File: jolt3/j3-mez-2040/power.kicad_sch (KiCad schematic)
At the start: 9 parts, among them J29 USB_C_Receptacle_USB2.0_14P, J30 Conn_ARM_JTAG_SWD_10, U2 AP2112-M3.3

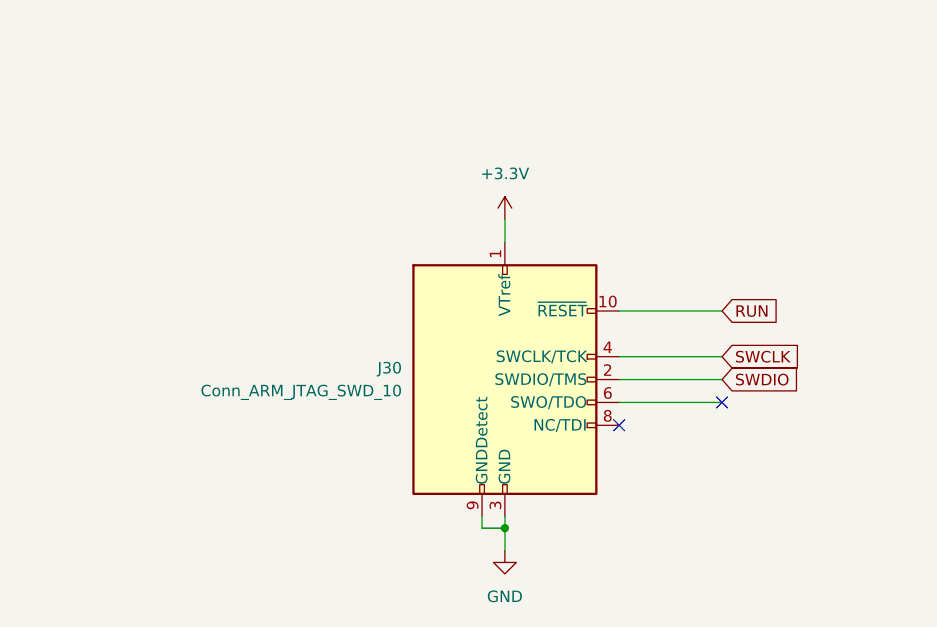
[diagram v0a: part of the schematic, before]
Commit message: Jolt 3: Rev A for 3 boards
Send Rev A out for jolt3-left, jolt3-right, and j3-mez-2040.
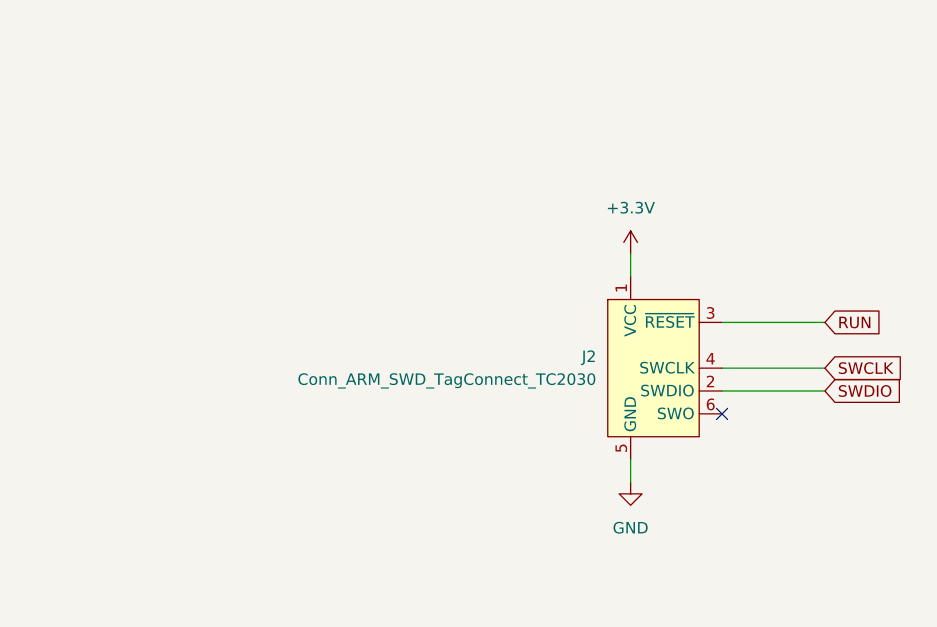
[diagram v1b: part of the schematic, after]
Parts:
- removed J30: Conn_ARM_JTAG_SWD_10, davidb-keyboard-foot:Cortex-M-Debug10, symbol David Brown Keyboard Parts:Conn_ARM_JTAG_SWD_10
- added J2: Conn_ARM_SWD_TagConnect_TC2030, Connector:Tag-Connect_TC2030-IDC-FP_2x03_P1.27mm_Vertical, symbol Connector:Conn_ARM_SWD_TagConnect_TC2030
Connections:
- net +3.3V: now also J2.1 (VCC)
- net GND: now also J2.5 (GND)
- net RUN: now also J2.3 (~{RESET})
- net SWCLK: now also J2.4 (SWCLK)
- net SWDIO: now also J2.2 (SWDIO)
- no-connect marks 3 -> 2
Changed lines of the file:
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@@
-	)
-	(junction
-		(at 156.21 135.89)
-		(diameter 0)
-		(color 0 0 0 0)
 	)
 	(junction
@@
 	)
 	(no_connect
-		(at 168.91 124.46)
+		(at 86.36 125.73)
 	)
 	(no_connect
-		(at 86.36 125.73)
-	)
-	(no_connect
-		(at 180.34 121.92)
+		(at 180.34 123.19)
 	)
 	(wire
@@
 	(wire
 		(pts
-			(xy 156.21 101.6) (xy 156.21 104.14)
+			(xy 170.18 105.41) (xy 170.18 107.95)
+		)
+		(stroke
+			(width 0)
+			(type default)
+		)
+	)
+	(wire
+		(pts
+			(xy 170.18 128.27) (xy 170.18 130.81)
 		)
 		(stroke
@@
 	(wire
 		(pts
-			(xy 168.91 111.76) (xy 180.34 111.76)
-		)
-		(stroke
-			(width 0)
-			(type default)
-		)
-	)
-	(wire
-		(pts
-			(xy 168.91 116.84) (xy 180.34 116.84)
-		)
-		(stroke
-			(width 0)
-			(type default)
-		)
-	)
-	(wire
-		(pts
-			(xy 156.21 135.89) (xy 156.21 138.43)
+			(xy 180.34 113.03) (xy 191.77 113.03)
+		)
+		(stroke
+			(width 0)
+			(type default)
+		)
+	)
+	(wire
+		(pts
+			(xy 180.34 118.11) (xy 191.77 118.11)
 		)
 		(stroke
@@
 	(wire
 		(pts
-			(xy 168.91 121.92) (xy 180.34 121.92)
-		)
-		(stroke
-			(width 0)
-			(type default)
-		)
-	)
-	(wire
-		(pts
 			(xy 78.74 133.35) (xy 78.74 134.62)
 		)
@@
 	(wire
 		(pts
-			(xy 153.67 134.62) (xy 153.67 135.89)
-		)
-		(stroke
-			(width 0)
-			(type default)
-		)
-	)
-	(wire
-		(pts
 			(xy 67.31 66.04) (xy 69.85 66.04)
 		)
@@
 	(wire
 		(pts
-			(xy 156.21 134.62) (xy 156.21 135.89)
-		)
-		(stroke
-			(width 0)
-			(type default)
-		)
-	)
-	(wire
-		(pts
 			(xy 69.85 66.04) (xy 69.85 63.5)
 		)
@@
 	(wire
 		(pts
-			(xy 153.67 135.89) (xy 156.21 135.89)
-		)
-		(stroke
-			(width 0)
-			(type default)
-		)
-	)
-	(wire
-		(pts
 			(xy 93.98 50.8) (xy 128.27 50.8)
 		)
@@
 	(wire
 		(pts
-			(xy 168.91 119.38) (xy 180.34 119.38)
+			(xy 180.34 120.65) (xy 191.77 120.65)
 		)
 		(stroke
@@
 	(global_label "SWCLK"
 		(shape input)
-		(at 180.34 116.84 0)
+		(at 191.77 118.11 0)
 		(fields_autoplaced yes)
 		(effects
@@
 		)
 		(property "Intersheetrefs" "${INTERSHEET_REFS}"
-			(at 189.5542 116.84 0)
+			(at 200.9842 118.11 0)
 			(effects
 				(font
@@
 	(global_label "SWDIO"
 		(shape input)
-		(at 180.34 119.38 0)
+		(at 191.77 120.65 0)
 		(fields_autoplaced yes)
 		(effects
@@
 		)
 		(property "Intersheetrefs" "${INTERSHEET_REFS}"
-			(at 189.1914 119.38 0)
+			(at 200.6214 120.65 0)
 			(effects
 				(font
@@
 	(global_label "RUN"
 		(shape input)
-		(at 180.34 111.76 0)
+		(at 191.77 113.03 0)
 		(fields_autoplaced yes)
 		(effects
@@
 		)
 		(property "Intersheetrefs" "${INTERSHEET_REFS}"
-			(at 187.2562 111.76 0)
+			(at 198.6862 113.03 0)
 			(effects
 				(font
@@
 	(symbol
 		(lib_id "power:GND")
-		(at 156.21 138.43 0)
+		(at 170.18 130.81 0)
 		(unit 1)
 		(exclude_from_sim no)
@@
 		(fields_autoplaced yes)
 		(property "Reference" "#PWR026"
-			(at 156.21 144.78 0)
+			(at 170.18 137.16 0)
 			(effects
 				(font
@@
 		)
 		(property "Value" "GND"
-			(at 156.21 143.51 0)
+			(at 170.18 135.89 0)
 			(effects
 				(font
@@
 		)
 		(property "Footprint" ""
-			(at 156.21 138.43 0)
+			(at 170.18 130.81 0)
 			(effects
 				(font
@@
 		)
 		(property "Datasheet" ""
-			(at 156.21 138.43 0)
+			(at 170.18 130.81 0)
 			(effects
 				(font
@@
 		)
 		(property "Description" "Power symbol creates a global label with name \"GND\" , ground"
-			(at 156.21 138.43 0)
+			(at 170.18 130.81 0)
 			(effects
 				(font
@@
 	)
 	(symbol
+		(lib_id "Connector:Conn_ARM_SWD_TagConnect_TC2030")
+		(at 172.72 118.11 0)
+		(unit 1)
+		(exclude_from_sim no)
+		(in_bom no)
+		(on_board yes)
+		(dnp no)
+		(fields_autoplaced yes)
+		(property "Reference" "J2"
+			(at 166.37 116.8399 0)
+			(effects
+				(font
+					(size 1.27 1.27)
+				)
+				(justify right)
+			)
+		)
+		(property "Value" "Conn_ARM_SWD_TagConnect_TC2030"
+			(at 166.37 119.3799 0)
+			(effects
+				(font
+					(size 1.27 1.27)
+				)
+				(justify right)
+			)
+		)
+		(property "Footprint" "Connector:Tag-Connect_TC2030-IDC-FP_2x03_P1.27mm_Vertical"
+			(at 172.72 135.89 0)
+			(effects
+				(font
+					(size 1.27 1.27)
+				)
+				(hide yes)
+			)
+		)
+		(property "Datasheet" "https://www.tag-connect.com/wp-content/uploads/bsk-pdf-manager/TC2030-CTX_1.pdf"
+			(at 172.72 133.35 0)
+			(effects
+				(font
+					(size 1.27 1.27)
+				)
+				(hide yes)
+			)
+		)
+		(property "Description" "Tag-Connect ARM Cortex SWD JTAG connector, 6 pin"
+			(at 172.72 118.11 0)
+			(effects
+				(font
+					(size 1.27 1.27)
+				)
+				(hide yes)
+			)
+		)
+		(pin "4"
+		)
+		(pin "1"
+		)
+		(pin "5"
+		)
+		(pin "3"
+		)
+		(pin "2"
+		)
+		(pin "6"
+		)
+		(instances
+			(project ""
+				(path "/5e404b8e-7f18-4204-bb67-87c83d2db771/a1c76de4-528d-42ab-822c-b4e73696ff22"
+					(reference "J2")
+					(unit 1)
+				)
+			)
+		)
+	)
+	(symbol
 		(lib_id "power:GND")
 		(at 52.07 88.9 0)
@@
 	(symbol
 		(lib_id "power:+3.3V")
-		(at 156.21 101.6 0)
+		(at 170.18 105.41 0)
 		(unit 1)
 		(exclude_from_sim no)
@@
 		(fields_autoplaced yes)
 		(property "Reference" "#PWR025"
-			(at 156.21 105.41 0)
+			(at 170.18 109.22 0)
 			(effects
 				(font
@@
 		)
 		(property "Value" "+3.3V"
-			(at 156.21 96.52 0)
+			(at 170.18 100.33 0)
 			(effects
 				(font
@@
 		)
 		(property "Footprint" ""
-			(at 156.21 101.6 0)
+			(at 170.18 105.41 0)
 			(effects
 				(font
@@
 		)
 		(property "Datasheet" ""
-			(at 156.21 101.6 0)
+			(at 170.18 105.41 0)
 			(effects
 				(font
@@
 		)
 		(property "Description" "Power symbol creates a global label with name \"+3.3V\""
-			(at 156.21 101.6 0)
+			(at 170.18 105.41 0)
 			(effects
 				(font
@@
 					(unit 1)
 				)
-			)
-		)
-	)
-	(symbol
-		(lib_id "David Brown Keyboard Parts:Conn_ARM_JTAG_SWD_10")
-		(at 156.21 119.38 0)
-		(unit 1)
-		(exclude_from_sim no)
-		(in_bom yes)
-		(on_board yes)
-		(dnp no)
-		(fields_autoplaced yes)
-		(property "Reference" "J30"
-			(at 144.78 118.1099 0)
-			(effects
-				(font
-					(size 1.27 1.27)
-				)
-				(justify right)
-			)
-		)
-		(property "Value" "Conn_ARM_JTAG_SWD_10"
-			(at 144.78 120.6499 0)
-			(effects
-				(font
-					(size 1.27 1.27)
-				)
-				(justify right)
-			)
-		)
-		(property "Footprint" "davidb-keyboard-foot:Cortex-M-Debug10"
-			(at 156.21 119.38 0)
-			(effects
-				(font
-					(size 1.27 1.27)
-				)
-				(hide yes)
-			)
-		)
-		(property "Datasheet" "http://infocenter.arm.com/help/topic/com.arm.doc.ddi0314h/DDI0314H_coresight_components_trm.pdf"
-			(at 147.32 151.13 90)
-			(effects
-				(font
-					(size 1.27 1.27)
-				)
-				(hide yes)
-			)
-		)
-		(property "Description" "Cortex Debug Connector, standard ARM Cortex-M SWD and JTAG interface"
-			(at 156.21 119.38 0)
-			(effects
-				(font
-					(size 1.27 1.27)
-				)
-				(hide yes)
-			)
-		)
-		(pin "4"
-		)
-		(pin "8"
-		)
-		(pin "2"
-		)
-		(pin "9"
-		)
-		(pin "3"
-		)
-		(pin "6"
-		)
-		(pin "7"
-		)
-		(pin "1"
-		)
-		(pin "5"
-		)
-		(pin "10"
-		)
-		(instances
-			(project ""
-				(path "/5e404b8e-7f18-4204-bb67-87c83d2db771/a1c76de4-528d-42ab-822c-b4e73696ff22"
-					(reference "J30")
-					(unit 1)
-				)
